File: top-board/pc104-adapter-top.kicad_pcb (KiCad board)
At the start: 4 copper layers, 92.8 x 32.6 mm, 14 parts, among them J1 Conn_01x13_Male, J10 SAMTEC-TSW-126-07-X-D, J2 Conn_01x13_Male, J3 Conn_01x13_Male, J4 Conn_01x13_Male, J5 Conn_01x13_Male, J6 Conn_01x13_Male, J7 Conn_01x13_Male, J8 Conn_01x13_Male, J9 SAMTEC-TSW-126-07-X-D

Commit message: top-board: layout: Removing all tracks and inverting the connectors #7
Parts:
- G***: moved to F.Cu
- J1, J2, J3, J4, J5, J6, J7, J8, REF**: moved to B.Cu
- turned G*** to 0 degrees
- turned J1 to 180 degrees
- turned J2 to 180 degrees
- turned J3 to 180 degrees
- turned J4 to 180 degrees
- turned J5 to 180 degrees
- turned J6 to 180 degrees
- turned J7 to 180 degrees
- turned J8 to 180 degrees
- turned REF** to 180 degrees
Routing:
- net /A12: track 33.6 -> 0.00 mm
- net /A8: track 33.6 -> 0.00 mm
- net /A10: track 33.6 -> 0.00 mm
- net /A4: track 33.5 -> 0.00 mm
- net /A6: track 33.5 -> 0.00 mm, vias 1 -> 0
- net /A2: track 33.5 -> 0.00 mm
- net /A40: track 33.1 -> 0.00 mm
- net /A42: track 33.1 -> 0.00 mm
- net /A44: track 33.1 -> 0.00 mm
- net /A46: track 33.0 -> 0.00 mm
- net /A48: track 33.0 -> 0.00 mm
- net /A50: track 33.0 -> 0.00 mm
- net /A52: track 33.0 -> 0.00 mm
- net /A13: track 31.6 -> 0.00 mm
- net /A11: track 31.6 -> 0.00 mm
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
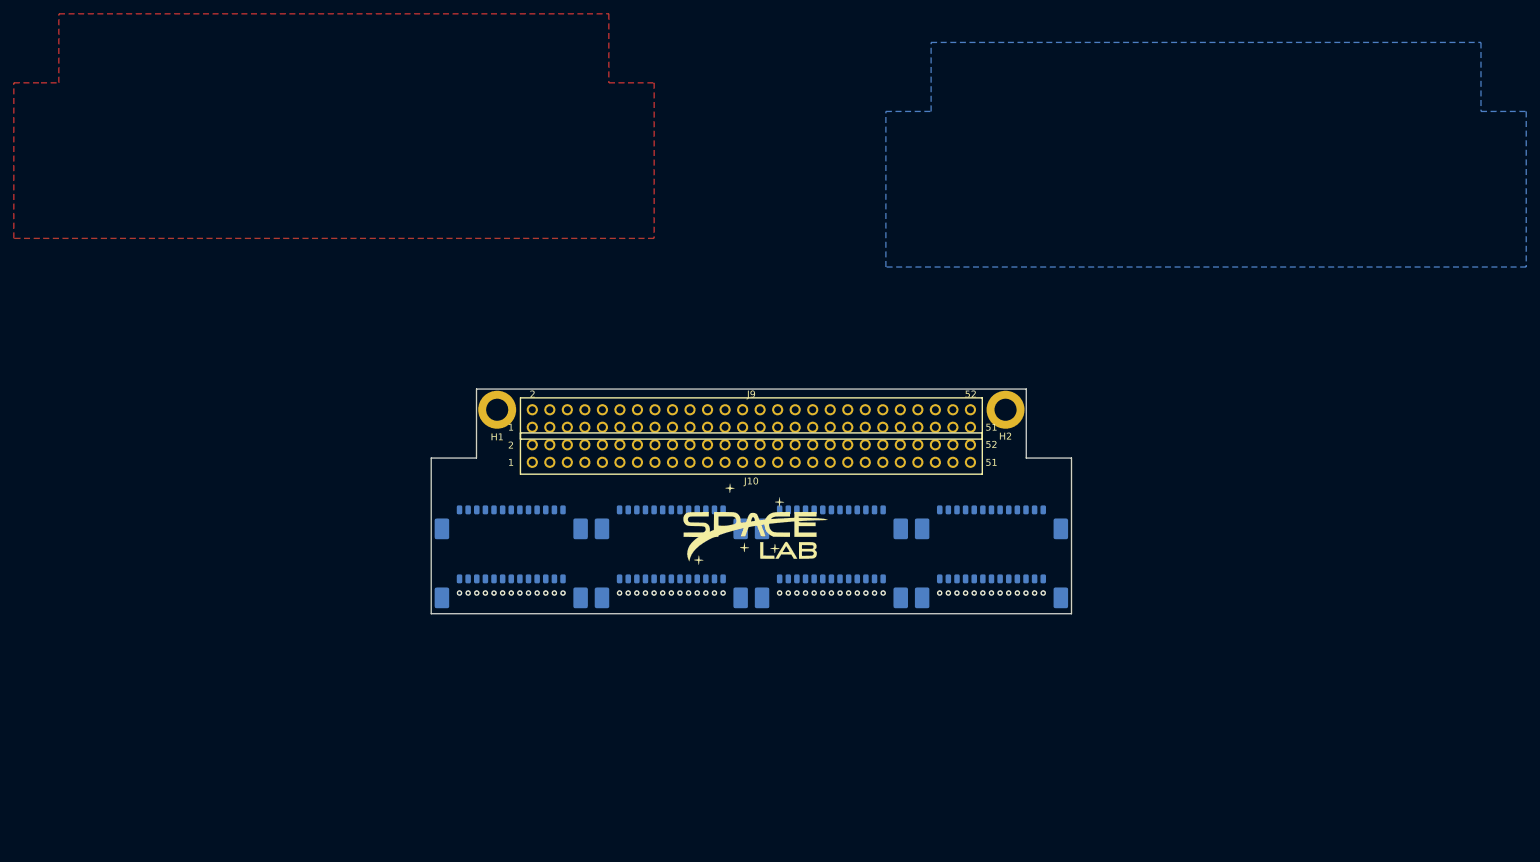
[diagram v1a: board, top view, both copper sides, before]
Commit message: top-board: Schematic and PCB layout #7
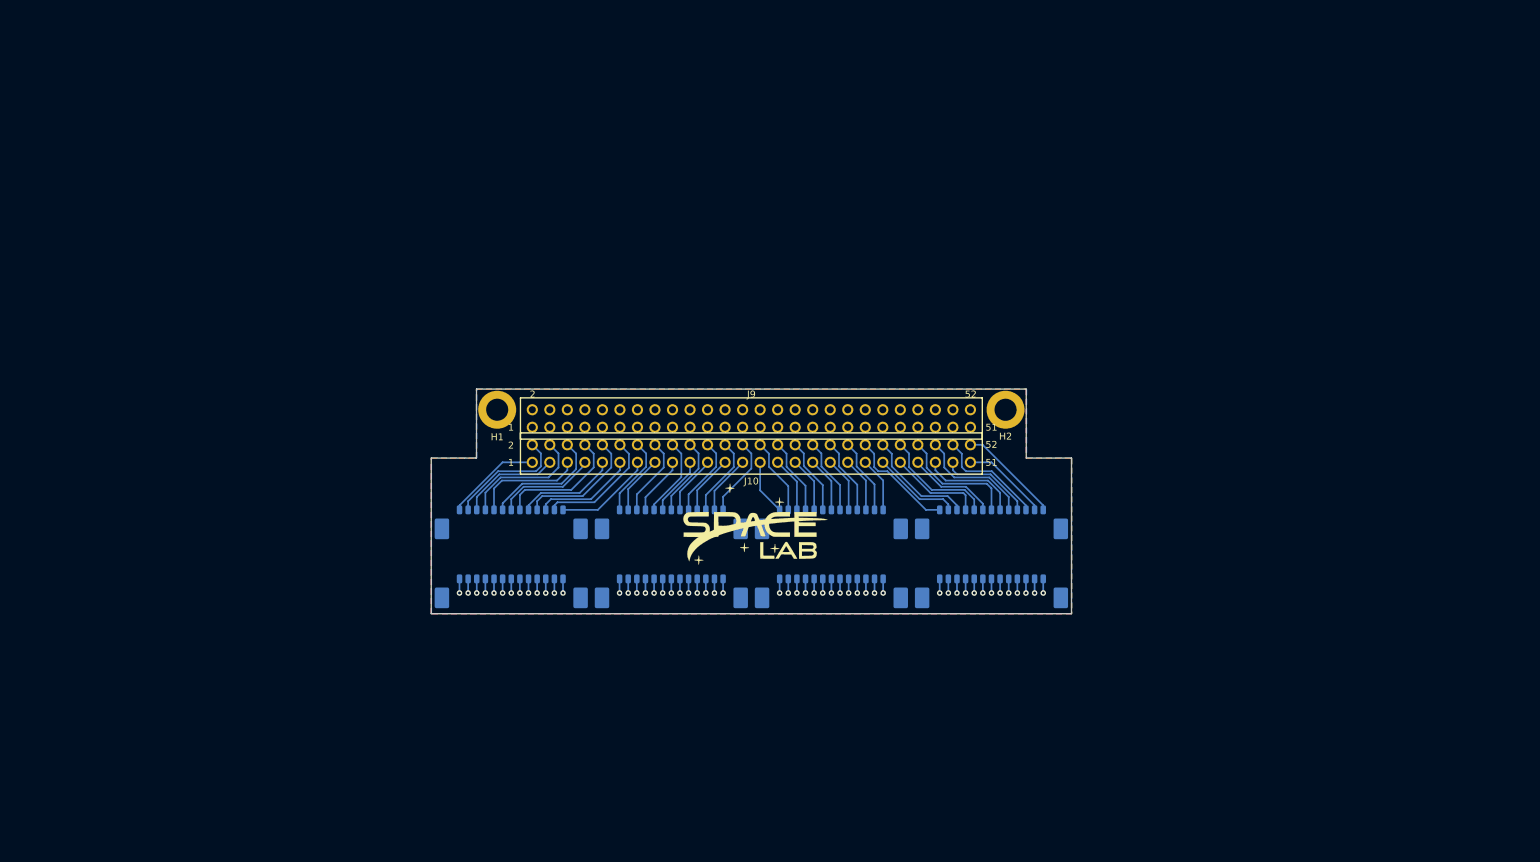
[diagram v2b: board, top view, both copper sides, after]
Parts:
- J10, J9: value SAMTEC-TSW-126-07-X-D -> SAMTEC-SSW-126-01-G-D
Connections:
- J1 pad 1: /A1 -> /A13
- J1 pad 10: /A10 -> /A4
- J1 pad 11: /A11 -> /A3
- J1 pad 12: /A12 -> /A2
- J1 pad 13: /A13 -> /A1
- J1 pad 2: /A2 -> /A12
- J1 pad 3: /A3 -> /A11
- J1 pad 4: /A4 -> /A10
- J1 pad 5: /A5 -> /A9
- J1 pad 6: /A6 -> /A8
- J1 pad 8: /A8 -> /A6
- J1 pad 9: /A9 -> /A5
- J2 pad 1: /A14 -> /A26
- J2 pad 10: /A23 -> /A17
- J2 pad 11: /A24 -> /A16
- J2 pad 12: /A25 -> /A15
- J2 pad 13: /A26 -> /A14
- J2 pad 2: /A15 -> /A25
- J2 pad 3: /A16 -> /A24
- J2 pad 4: /A17 -> /A23
- J2 pad 5: /A18 -> /A22
- J2 pad 6: /A19 -> /A21
- J2 pad 8: /A21 -> /A19
- J2 pad 9: /A22 -> /A18
- J3 pad 1: /A27 -> /A39
- J3 pad 10: /A36 -> /A30
- J3 pad 11: /A37 -> /A29
- J3 pad 12: /A38 -> /A28
- J3 pad 13: /A39 -> /A27
- J3 pad 2: /A28 -> /A38
- J3 pad 3: /A29 -> /A37
- J3 pad 4: /A30 -> /A36
- J3 pad 5: /A31 -> /A35
- J3 pad 6: /A32 -> /A34
- J3 pad 8: /A34 -> /A32
- J3 pad 9: /A35 -> /A31
- J4 pad 1: /A40 -> /A52
- J4 pad 10: /A49 -> /A43
- J4 pad 11: /A50 -> /A42
- J4 pad 12: /A51 -> /A41
- J4 pad 13: /A52 -> /A40
- J4 pad 2: /A41 -> /A51
- J4 pad 3: /A42 -> /A50
- J4 pad 4: /A43 -> /A49
- J4 pad 5: /A44 -> /A48
- J4 pad 6: /A45 -> /A47
- J4 pad 8: /A47 -> /A45
- J4 pad 9: /A48 -> /A44
- J5 pad 1: /B1 -> /B13
- J5 pad 10: /B10 -> /B4
- J5 pad 11: /B11 -> /B3
- J5 pad 12: /B12 -> /B2
- J5 pad 13: /B13 -> /B1
- J5 pad 2: /B2 -> /B12
- J5 pad 3: /B3 -> /B11
- J5 pad 4: /B4 -> /B10
- J5 pad 5: /B5 -> /B9
- J5 pad 6: /B6 -> /B8
- J5 pad 8: /B8 -> /B6
- J5 pad 9: /B9 -> /B5
- J6 pad 1: /B14 -> /B26
- J6 pad 10: /B23 -> /B17
- J6 pad 11: /B24 -> /B16
- J6 pad 12: /B25 -> /B15
- J6 pad 13: /B26 -> /B14
- J6 pad 2: /B15 -> /B25
- J6 pad 3: /B16 -> /B24
- J6 pad 4: /B17 -> /B23
- J6 pad 5: /B18 -> /B22
- J6 pad 6: /B19 -> /B21
- J6 pad 8: /B21 -> /B19
- J6 pad 9: /B22 -> /B18
- J7 pad 1: /B27 -> /B39
- J7 pad 10: /B36 -> /B30
- J7 pad 11: /B37 -> /B29
- J7 pad 12: /B38 -> /B28
- J7 pad 13: /B39 -> /B27
- J7 pad 2: /B28 -> /B38
- J7 pad 3: /B29 -> /B37
- J7 pad 4: /B30 -> /B36
- J7 pad 5: /B31 -> /B35
- J7 pad 6: /B32 -> /B34
- J7 pad 8: /B34 -> /B32
- J7 pad 9: /B35 -> /B31
- J8 pad 1: /B40 -> /B52
- J8 pad 10: /B49 -> /B43
- J8 pad 11: /B50 -> /B42
- J8 pad 12: /B51 -> /B41
- J8 pad 13: /B52 -> /B40
- J8 pad 2: /B41 -> /B51
- J8 pad 3: /B42 -> /B50
- J8 pad 4: /B43 -> /B49
- J8 pad 5: /B44 -> /B48
- J8 pad 6: /B45 -> /B47
- J8 pad 8: /B47 -> /B45
- J8 pad 9: /B48 -> /B44
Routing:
- net /A40: track 0.00 -> 33.1 mm
- net /A42: track 0.00 -> 33.1 mm
- net /A44: track 0.00 -> 33.1 mm
- net /A46: track 0.00 -> 33.0 mm
- net /A48: track 0.00 -> 33.0 mm
- net /A50: track 0.00 -> 33.0 mm
- net /A52: track 0.00 -> 33.0 mm
- net /A12: track 0.00 -> 32.5 mm
- net /A10: track 0.00 -> 32.5 mm
- net /A8: track 0.00 -> 32.5 mm
- net /A6: track 0.00 -> 32.5 mm, vias 0 -> 1
- net /A4: track 0.00 -> 32.5 mm
- net /A2: track 0.00 -> 32.5 mm
- net /A13: track 0.00 -> 30.5 mm
- net /A11: track 0.00 -> 30.5 mm
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
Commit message: top_board: layout: Adding labels to identify the PicoBlade connector pins #3 #7 #9
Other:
- board text added: "H1.1"
- board text added: "H1.13"
- board text added: "H1.14"
- board text added: "H1.26"
- board text added: "H1.27"
- board text added: "H1.39"
- board text added: "H1.40"
- board text added: "H1.52"
- board text added: "H2.1"
- board text added: "H2.13"
- board text added: "H2.14"
- board text added: "H2.26"
- board text added: "H2.27"
- board text added: "H2.39"
- board text added: "H2.40"
- board text added: "H2.52"

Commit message: top-board: layout: Fixing the PC-104 outline (silk screen) and adding a label with the board name and version #3 #7
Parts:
- removed REF**: OSHW-Symbol_6.7x6mm_SilkScreen, Symbol:OSHW-Symbol_6.7x6mm_SilkScreen
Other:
- board text added: "PC-104 Adapter (Top) v1.0"

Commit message: top-board: Version 2.0 #13
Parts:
- added H3: MountingHole_Pad, MountingHole:MountingHole_3.2mm_M3_ISO14580_Pad, F.Cu at (105.3, 140.9)
- added H4: MountingHole_Pad, MountingHole:MountingHole_3.2mm_M3_ISO14580_Pad, F.Cu at (185.4, 140.9)
- moved J1 29.5 mm to (119.7, 83.0), turned to 90 degrees
- moved J2 28.2 mm to (140.7, 83.0), turned to 90 degrees
- moved H2 27.1 mm to (182.8, 55.1)
- moved H1 27.1 mm to (109.2, 55.1)
- moved J10 27.1 mm to (146.0, 61.5)
- moved J9 27.1 mm to (146.0, 56.4)
- moved J3 27.0 mm to (161.8, 83.0), turned to 270 degrees
- moved J4 23.2 mm to (172.3, 83.0), turned to 270 degrees
- moved G*** 18.7 mm to (146.6, 81.0)
- moved J8 17.7 mm to (182.8, 83.0), turned to 270 degrees
- moved J5 15.3 mm to (109.2, 83.0), turned to 90 degrees
- moved J6 14.3 mm to (130.2, 83.0), turned to 90 degrees
- moved J7 13.6 mm to (151.3, 83.0), turned to 270 degrees
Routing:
- net GND: track 0.00 -> 92.0 mm, vias 0 -> 2
- net /B13: track 14.3 -> 43.9 mm
- net /B25: track 8.58 -> 36.1 mm, vias 0 -> 1
- net /B44: track 16.7 -> 43.4 mm
- net /B26: track 11.7 -> 36.9 mm, vias 0 -> 1
- net /B40: track 15.8 -> 38.8 mm, vias 0 -> 1
- net /B24: track 11.6 -> 33.1 mm, vias 0 -> 1
- net /B41: track 12.8 -> 34.2 mm, vias 0 -> 1
- net /B23: track 8.57 -> 29.8 mm, vias 0 -> 1
- net /B27: track 8.07 -> 29.0 mm
- net /B12: track 17.6 -> 38.2 mm, vias 0 -> 1
- net /B28: track 11.1 -> 30.6 mm
- net /B42: track 16.1 -> 34.7 mm, vias 0 -> 1
- net /B29: track 8.05 -> 26.5 mm
- net /B30: track 11.1 -> 29.4 mm, vias 0 -> 1
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- added copper zone on F.Cu, net GND
- removed copper zone on F.Cu, net (none)
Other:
- board size 92.8 x 32.6 mm -> 86.1 x 91.8 mm
- board text added: "PC-104 Adapter (Top) v2.0"
- board text removed: "PC-104 Adapter (Top) v1.0"

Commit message: top-board: Adding the Open Hardware logo #13
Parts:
- added REF**: OSHW-Logo_7.5x8mm_SilkScreen, Symbol:OSHW-Logo_7.5x8mm_SilkScreen, F.Cu at (146.6, 95.4)
